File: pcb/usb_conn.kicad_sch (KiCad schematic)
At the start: 39 parts, among them J2 CONN_USBC_RCPT_USB2.0_USB4085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, Q2 NFET_60V_0A5_2N7002KT1G, U8 IC_FTDI_FT231XS, U9 IC_LSW_TI_TPS2552D

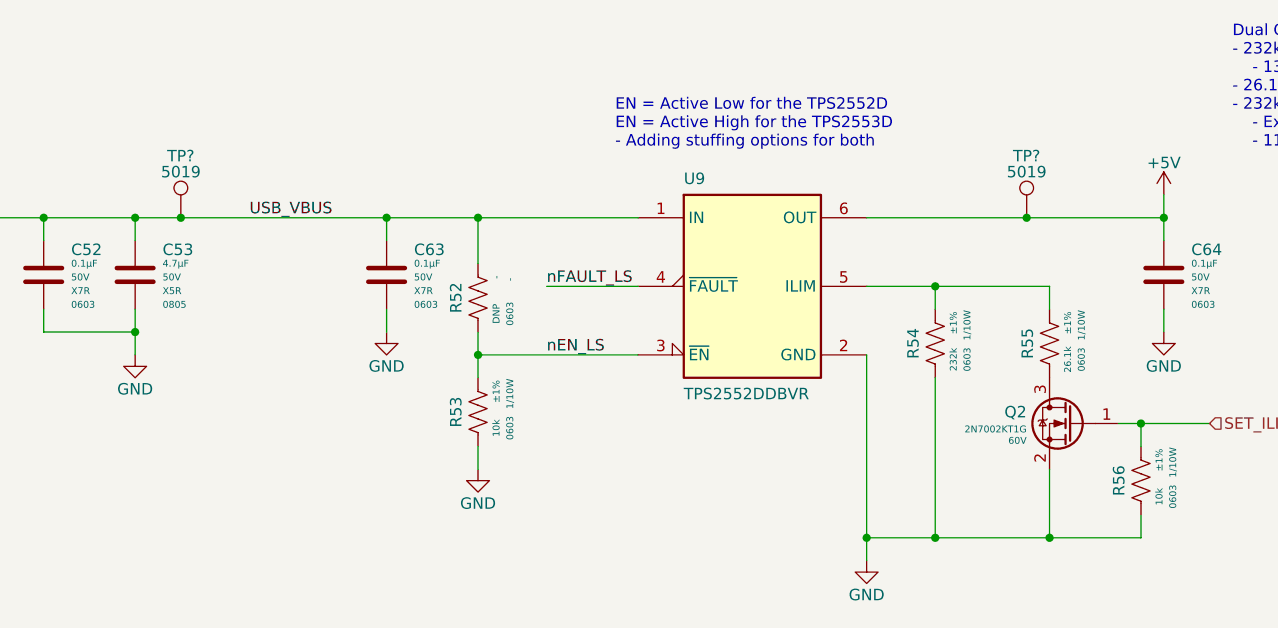
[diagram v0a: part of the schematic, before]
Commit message: Fixed a bunch of footprints and added missing 3D models
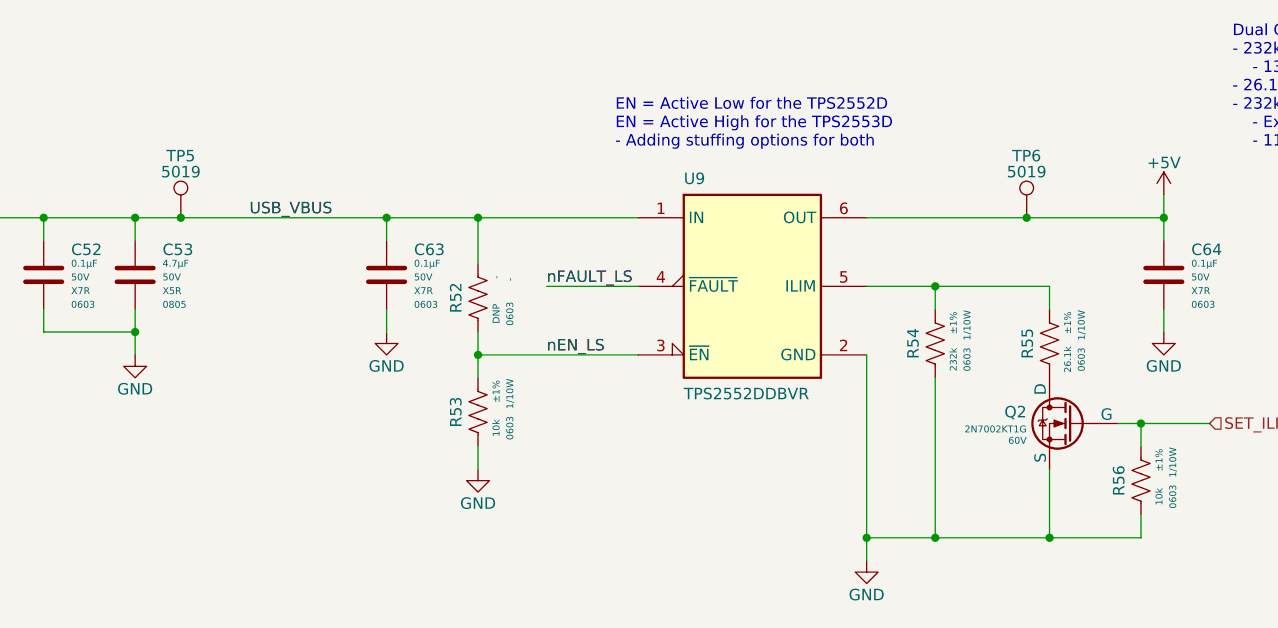
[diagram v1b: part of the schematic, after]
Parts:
- gave numbers to parts that had none: 2
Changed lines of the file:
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@@
   (symbol (lib_id ".arjun:TP_KEYSTONE_5019") (at 91.44 35.56 0) (unit 1)
     (in_bom yes) (on_board yes)
-    (property "Reference" "TP?" (id 0) (at 91.44 28.702 0))
+    (property "Reference" "TP5" (id 0) (at 91.44 28.702 0))
     (property "Value" "TP_KEYSTONE_5019" (id 1) (at 105.41 22.86 0)
       (effects (font (size 1.27 1.27)) (justify left) hide)
@@
   (symbol (lib_id ".arjun:TP_KEYSTONE_5019") (at 185.42 35.56 0) (unit 1)
     (in_bom yes) (on_board yes)
-    (property "Reference" "TP?" (id 0) (at 185.42 28.702 0))
+    (property "Reference" "TP6" (id 0) (at 185.42 28.702 0))
     (property "Value" "TP_KEYSTONE_5019" (id 1) (at 199.39 22.86 0)
       (effects (font (size 1.27 1.27)) (justify left) hide)

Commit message: Started layout!! 180V boost mostly laid out
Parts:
- C50: DNP DNP -> (none); now not fitted; now in the parts list
- R40: symbol arjun_symbols:RES_0R_1/8W_0805 -> arjun_symbols:RES_0R_1/8W_0805
- R41, R42: symbol arjun_symbols:RES_5K11_1P_1/10W_0603 -> arjun_symbols:RES_5K11_1P_1/10W_0603
- R47, R48: symbol .arjun:RES_27R_1P_1/10W_0603 -> .arjun:RES_27R_1P_1/10W_0603
- R49, R53, R56: symbol .arjun:RES_10K_1P_1/10W_0603 -> .arjun:RES_10K_1P_1/10W_0603
- R50: symbol .arjun:RES_1K5_1P_1/10W_0603 -> .arjun:RES_1K5_1P_1/10W_0603
- R51: symbol .arjun:RES_698R_1P_1/10W_0603 -> .arjun:RES_698R_1P_1/10W_0603
- R54: symbol .arjun:RES_232K_1P_1/10W_0603 -> .arjun:RES_232K_1P_1/10W_0603
- R55: symbol .arjun:RES_26K1_1P_1/10W_0603 -> .arjun:RES_26K1_1P_1/10W_0603
- R57: symbol .arjun:RES_3K3_1P_1/10W_0603 -> .arjun:RES_3K3_1P_1/10W_0603

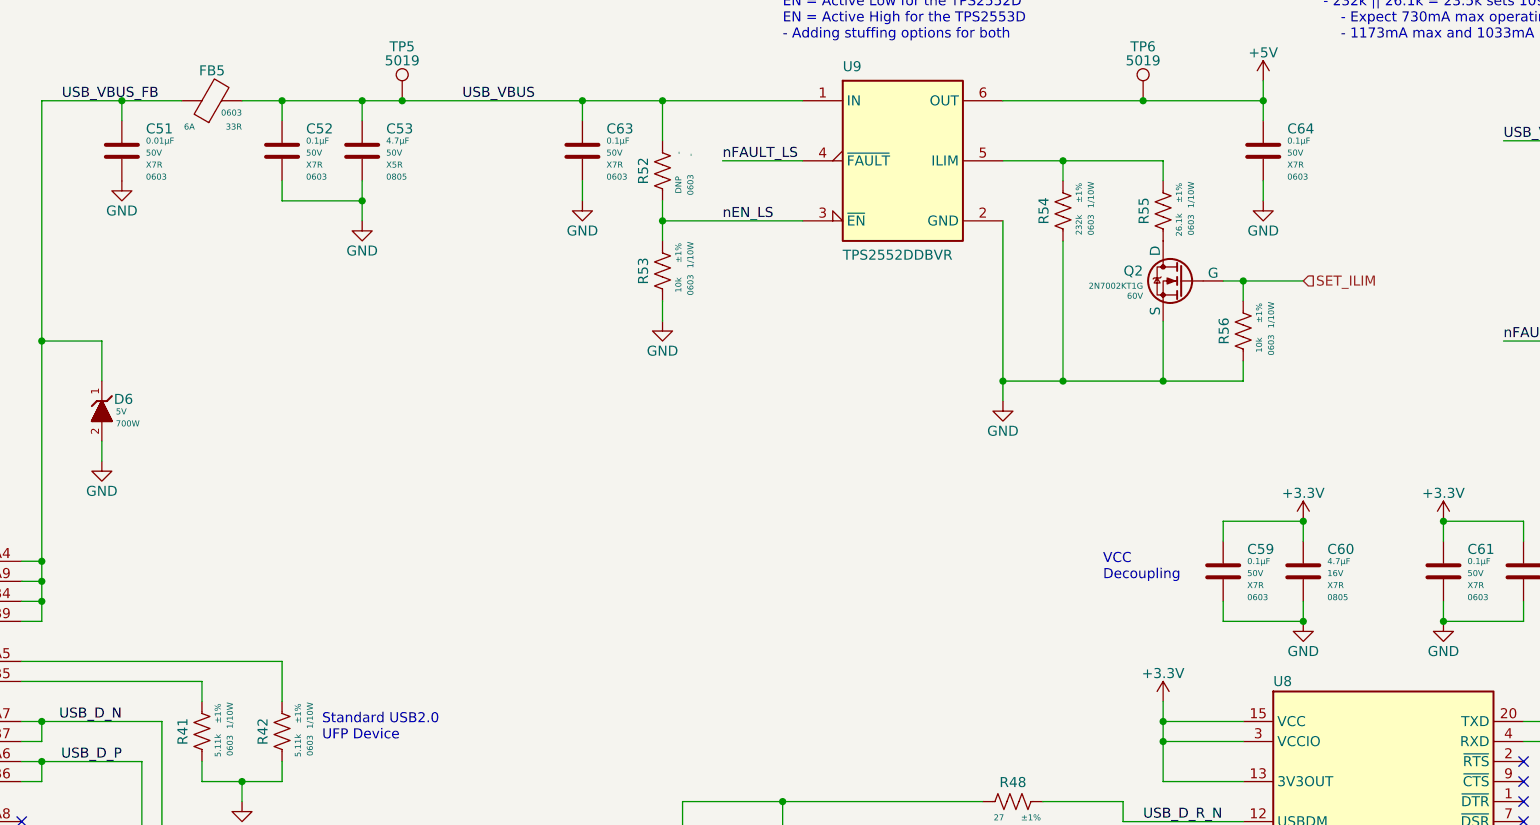
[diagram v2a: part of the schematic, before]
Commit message: Placement V1. Want to try and centre the board on the nixies vertically. Saving progress before trying out different placements.
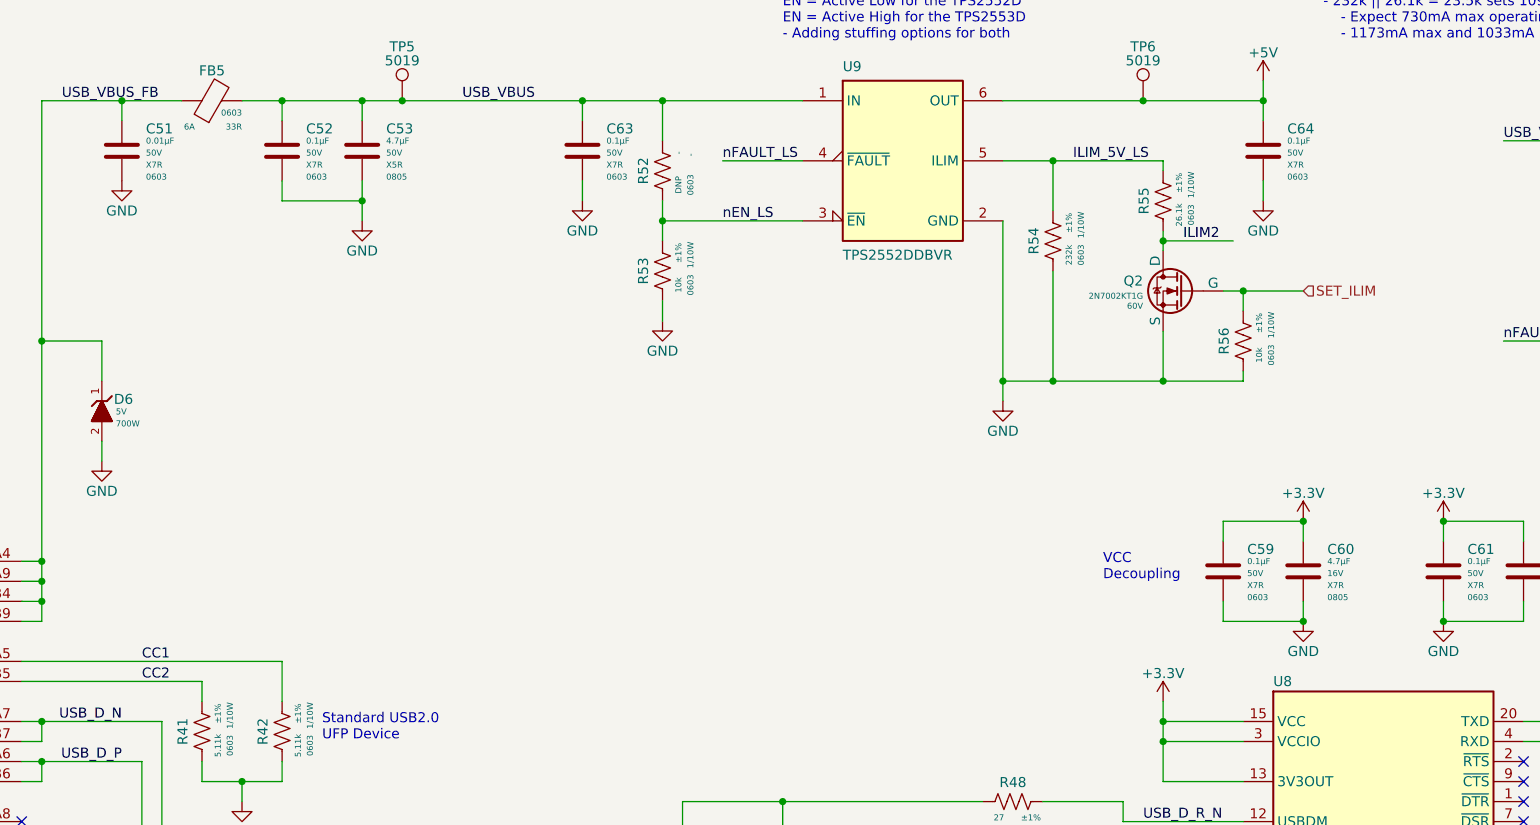
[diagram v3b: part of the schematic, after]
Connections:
- net ILIM_5V_LS: now reaches R54.1, R55.1, U9.5 (ILIM)
- net CC1: now reaches J2.A5 (CC1), R42.1
- net CC2: now reaches J2.B5 (CC2), R41.1
- net ILIM2: now reaches Q2.3 (D), R55.2
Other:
- moved on the sheet: Q2, R54, R55, R56

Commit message: Routing progress! Maybe 30% done.
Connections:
- net UART_BL_RX renamed UART1_BL_RX
- net UART_BL_TX renamed UART1_BL_TX
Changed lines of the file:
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@@
 		)
 	)
-	(hierarchical_label "UART_BL_TX"
+	(hierarchical_label "UART1_BL_TX"
 		(shape input)
 		(at 248.92 116.84 0)
@@
 		)
 	)
-	(hierarchical_label "UART_BL_RX"
+	(hierarchical_label "UART1_BL_RX"
 		(shape output)
 		(at 248.92 114.3 0)
@@
 		)
 	)
+	(netclass_flag ""
+		(length 2.54)
+		(shape round)
+		(at 82.55 139.7 0)
+		(fields_autoplaced yes)
+		(effects
+			(font
+				(size 1.27 1.27)
+			)
+			(justify left bottom)
+		)
+		(property "Netclass" "USB"
+			(at 83.2485 137.16 0)
+			(effects
+				(font
+					(size 1.27 1.27)
+					(italic yes)
+				)
+				(justify left)
+			)
+		)
+	)
+	(netclass_flag ""
+		(length 2.54)
+		(shape round)
+		(at 82.55 142.24 180)
+		(fields_autoplaced yes)
+		(effects
+			(font
+				(size 1.27 1.27)
+			)
+			(justify right bottom)
+		)
+		(property "Netclass" "USB"
+			(at 83.2485 144.78 0)
+			(effects
+				(font
+					(size 1.27 1.27)
+					(italic yes)
+				)
+				(justify left)
+			)
+		)
+	)
+	(netclass_flag ""
+		(length 2.54)
+		(shape round)
+		(at 176.53 124.46 0)
+		(fields_autoplaced yes)
+		(effects
+			(font
+				(size 1.27 1.27)
+			)
+			(justify left bottom)
+		)
+		(property "Netclass" "USB"
+			(at 177.2285 121.92 0)
+			(effects
+				(font
+					(size 1.27 1.27)
+					(italic yes)
+				)
+				(justify left)
+			)
+		)
+	)
+	(netclass_flag ""
+		(length 2.54)
+		(shape round)
+		(at 176.53 132.08 0)
+		(fields_autoplaced yes)
+		(effects
+			(font
+				(size 1.27 1.27)
+			)
+			(justify left bottom)
+		)
+		(property "Netclass" "USB"
+			(at 177.2285 129.54 0)
+			(effects
+				(font
+					(size 1.27 1.27)
+					(italic yes)
+				)
+				(justify left)
+			)
+		)
+	)

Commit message: Some silk additions
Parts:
- TP5: value TP_KEYSTONE_5019 -> VBUS
- TP6: value TP_KEYSTONE_5019 -> 5V
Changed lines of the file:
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@@
 			)
 		)
-		(property "Value" "TP_KEYSTONE_5019"
+		(property "Value" "VBUS"
 			(at 105.41 22.86 0)
 			(effects
@@
 			)
 		)
-		(property "Value" "TP_KEYSTONE_5019"
+		(property "Value" "5V"
 			(at 199.39 22.86 0)
 			(effects

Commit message: Some minor tweaks and generated gerbers
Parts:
- R52: now not fitted
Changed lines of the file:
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@@
 		(in_bom yes)
 		(on_board yes)
-		(dnp no)
+		(dnp yes)
 		(property "Reference" "R52"
 			(at 121.285 44.45 90)

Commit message: Generated outputs for built round 2
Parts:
- removed D4: D_TVS_BI_3V6_20W_3-XFDFN, arjun_footprints:DIO_ESD122DMYR, symbol .arjun:D_TVS_BI_3V6_20W_3-XFDFN
- added D4: D_TVS_UNI_5V_300W_SOT-523, arjun_footprints:SOT-523_SEMTECH, symbol arjun_lib:D_TVS_UNI_5V_300W_SOT-523
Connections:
- net GND: now also D4.3
- net USB_D_N: now also D4.2
- net USB_D_P: now also D4.1
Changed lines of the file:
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@@
 	)
 	(junction
-		(at 66.04 142.24)
+		(at 66.04 139.7)
 		(diameter 0)
 		(color 0 0 0 0)
@@
 	)
 	(junction
-		(at 71.12 139.7)
+		(at 71.12 142.24)
 		(diameter 0)
 		(color 0 0 0 0)
@@
 	(wire
 		(pts
+			(xy 71.12 142.24) (xy 71.12 144.78)
+		)
+		(stroke
+			(width 0)
+			(type default)
+		)
+	)
+	(wire
+		(pts
 			(xy 173.99 71.12) (xy 173.99 57.15)
 		)
@@
 	(wire
 		(pts
-			(xy 71.12 139.7) (xy 71.12 144.78)
-		)
-		(stroke
-			(width 0)
-			(type default)
-		)
-	)
-	(wire
-		(pts
 			(xy 124.46 48.26) (xy 124.46 50.8)
 		)
@@
 	(wire
 		(pts
-			(xy 66.04 142.24) (xy 58.42 142.24)
-		)
-		(stroke
-			(width 0)
-			(type default)
-		)
-	)
-	(wire
-		(pts
 			(xy 173.99 43.18) (xy 173.99 49.53)
 		)
@@
 	(wire
 		(pts
+			(xy 66.04 139.7) (xy 127 139.7)
+		)
+		(stroke
+			(width 0)
+			(type default)
+		)
+	)
+	(wire
+		(pts
 			(xy 256.54 137.16) (xy 264.16 137.16)
 		)
@@
 	(wire
 		(pts
-			(xy 127 139.7) (xy 71.12 139.7)
+			(xy 60.96 139.7) (xy 66.04 139.7)
 		)
 		(stroke
@@
 	(wire
 		(pts
-			(xy 129.54 142.24) (xy 66.04 142.24)
+			(xy 129.54 142.24) (xy 71.12 142.24)
 		)
 		(stroke
@@
 	(wire
 		(pts
-			(xy 198.12 121.92) (xy 187.96 121.92)
+			(xy 58.42 142.24) (xy 71.12 142.24)
 		)
 		(stroke
@@
 	(wire
 		(pts
-			(xy 198.12 59.69) (xy 205.74 59.69)
+			(xy 198.12 121.92) (xy 187.96 121.92)
 		)
 		(stroke
@@
 	(wire
 		(pts
-			(xy 149.86 144.78) (xy 149.86 147.32)
+			(xy 198.12 59.69) (xy 205.74 59.69)
 		)
 		(stroke
@@
 	(wire
 		(pts
-			(xy 66.04 142.24) (xy 66.04 144.78)
+			(xy 149.86 144.78) (xy 149.86 147.32)
 		)
 		(stroke
@@
 	(wire
 		(pts
-			(xy 71.12 139.7) (xy 60.96 139.7)
+			(xy 43.18 119.38) (xy 45.72 119.38)
 		)
 		(stroke
@@
 	(wire
 		(pts
-			(xy 43.18 119.38) (xy 45.72 119.38)
+			(xy 205.74 99.06) (xy 205.74 101.6)
 		)
 		(stroke
@@
 	(wire
 		(pts
-			(xy 205.74 99.06) (xy 205.74 101.6)
+			(xy 86.36 35.56) (xy 86.36 38.1)
 		)
 		(stroke
@@
 	(wire
 		(pts
-			(xy 86.36 35.56) (xy 86.36 38.1)
+			(xy 66.04 139.7) (xy 66.04 144.78)
 		)
 		(stroke
@@
 	)
 	(symbol
+		(lib_id "arjun_lib:D_TVS_UNI_5V_300W_SOT-523")
+		(at 66.04 144.78 0)
+		(unit 1)
+		(exclude_from_sim no)
+		(in_bom yes)
+		(on_board yes)
+		(dnp no)
+		(property "Reference" "D4"
+			(at 73.66 150.495 0)
+			(effects
+				(font
+					(size 1.27 1.27)
+				)
+				(justify left bottom)
+			)
+		)
+		(property "Value" "D_TVS_UNI_5V_300W_SOT-523"
+			(at 85.09 139.7 0)
+			(effects
+				(font
+					(size 1.27 1.27)
+				)
+				(justify left)
+				(hide yes)
+			)
+		)
+		(property "Footprint" "arjun_footprints:SOT-523_SEMTECH"
+			(at 86.36 154.94 0)
+			(effects
+				(font
+					(size 1.27 1.27)
+				)
+				(justify left)
+				(hide yes)
+			)
+		)
+		(property "Datasheet" "https://semtech.my.salesforce.com/sfc/p/#E0000000JelG/a/2R000000UtE2/eXIrX7HkoSLYp5yJlnqbpQTN03aeTkeFqOGu_CePrtY"
+			(at 85.09 152.4 0)
+			(effects
+				(font
+					(size 1.27 1.27)
+				)
+				(justify left)
+				(hide yes)
+			)
+		)
+		(property "Description" "20V Clamp 15A (8/20µs) Ipp Tvs Diode Surface Mount SC-75 (SOT523)"
+			(at 66.04 144.78 0)
+			(effects
+				(font
+					(size 1.27 1.27)
+				)
+				(hide yes)
+			)
+		)
+		(property "Manufacturer" "Semtech Corporation"
+			(at 85.09 142.24 0)
+			(effects
+				(font
+					(size 1.27 1.27)
+				)
+				(justify left)
+				(hide yes)
+			)
+		)
+		(property "ManufacturerPN" "RCLAMP0582BQTCT"
+			(at 85.09 144.78 0)
+			(effects
+				(font
+					(size 1.27 1.27)
+				)
+				(justify left)
+				(hide yes)
+			)
+		)
+		(property "Vendor" "Digi-Key"
+			(at 85.09 147.32 0)
+			(effects
+				(font
+					(size 1.27 1.27)
+				)
+				(justify left)
+				(hide yes)
+			)
+		)
+		(property "VendorPN" "RCLAMP0582BQTCTCT-ND"
+			(at 85.09 149.86 0)
+			(effects
+				(font
+					(size 1.27 1.27)
+				)
+				(justify left)
+				(hide yes)
+			)
+		)
+		(property "Vr" "5V"
+			(at 73.66 152.146 0)
+			(effects
+				(font
+					(size 0.762 0.762)
+				)
+				(justify left bottom)
+			)
+		)
+		(property "Power Peak Pulse" "300W"
+			(at 73.66 153.67 0)
+			(effects
+				(font
+					(size 0.762 0.762)
+				)
+				(justify left bottom)
+			)
+		)
+		(pin "3"
+		)
+		(pin "2"
+		)
+		(pin "1"
+		)
+		(instances
+			(project ""
+				(path "/962b4e87-b270-45b9-b05a-9c836fe2392e/c489a08b-e150-4d56-8df0-484cd36f24a0"
+					(reference "D4")
+					(unit 1)
+				)
+			)
+		)
+	)
+	(symbol
 		(lib_id "power:GND")
 		(at 139.7 147.32 0)
@@
 					(unit 1)
 				)
-			)
-		)
-	)
-	(symbol
-		(lib_id ".arjun:D_TVS_BI_3V6_20W_3-XFDFN")
-		(at 66.04 144.78 0)
-		(unit 1)
-		(exclude_from_sim no)
-		(in_bom yes)
-		(on_board yes)
-		(dnp no)
-		(property "Reference" "D4"
-			(at 73.66 150.495 0)
-			(effects
-				(font
-					(size 1.27 1.27)
-				)
-				(justify left bottom)
-			)
-		)
-		(property "Value" "D_TVS_BI_3V6_20W_3-XFDFN"
-			(at 85.09 139.7 0)
-			(effects
-				(font
-					(size 1.27 1.27)
-				)
-				(justify left)
-				(hide yes)
-			)
-		)
-		(property "Footprint" "arjun_footprints:DIO_ESD122DMYR"
-			(at 86.36 154.94 0)
-			(effects
-				(font
-					(size 1.27 1.27)
-				)
-				(justify left)
-				(hide yes)
-			)
-		)
-		(property "Datasheet" "https://www.ti.com/lit/ds/symlink/esd122.pdf?HQS=dis-dk-null-digikeymode-dsf-pf-null-wwe&ts=1721083848066&ref_url=https%253A%252F%252Fwww.ti.com%252Fgeneral%252Fdocs%252Fsuppproductinfo.tsp%253FdistId%253D10%2526gotoUrl%253Dhttps%253A%252F%252Fwww.ti.com%252Flit%252Fgpn%252Fesd122"
-			(at 85.09 152.4 0)
-			(effects
-				(font
-					(size 1.27 1.27)
-				)
-				(justify left)
-				(hide yes)
-			)
-		)
-		(property "Description" ""
-			(at 66.04 144.78 0)
-			(effects
-				(font
-					(size 1.27 1.27)
-				)
-				(hide yes)
-			)
-		)
-		(property "Manufacturer" "Texas Instruments"
-			(at 85.09 142.24 0)
-			(effects
-				(font
-					(size 1.27 1.27)
-				)
-				(justify left)
-				(hide yes)
-			)
-		)
-		(property "ManufacturerPN" "ESD122DMYR"
-			(at 85.09 144.78 0)
-			(effects
-				(font
-					(size 1.27 1.27)
-				)
-				(justify left)
-				(hide yes)
-			)
-		)
-		(property "Vendor" "Digi-Key"
-			(at 85.09 147.32 0)
-			(effects
-				(font
-					(size 1.27 1.27)
-				)
-				(justify left)
-				(hide yes)
-			)
-		)
-		(property "VendorPN" "296-47120-1-ND"
-			(at 85.09 149.86 0)
-			(effects
-				(font
-					(size 1.27 1.27)
-				)
-				(justify left)
-				(hide yes)
-			)
-		)
-		(property "Vr" "3.6V"
-			(at 73.66 152.146 0)
-			(effects
-				(font
-					(size 0.762 0.762)
-				)
-				(justify left bottom)
-			)
-		)
-		(property "Power Peak Pulse" "20W"
-			(at 73.66 153.67 0)
-			(effects
-				(font
-					(size 0.762 0.762)
-				)
-				(justify left bottom)
-			)
-		)
-		(pin "1"
-		)
-		(pin "2"
-		)
-		(pin "3"
-		)
-		(instances
-			(project ""
-				(path "/962b4e87-b270-45b9-b05a-9c836fe2392e/c489a08b-e150-4d56-8df0-484cd36f24a0"
-					(reference "D4")
-					(unit 1)
-				)
